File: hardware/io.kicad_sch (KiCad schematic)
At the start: 0 parts

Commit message: Almost everything
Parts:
- added D1, D3: 1N4007, Diode_THT:D_DO-41_SOD81_P10.16mm_Horizontal, symbol Diode:1N4007
- added Q4, Q5: NPN, symbol Simulation_SPICE:NPN
- added R27, R29, R33, R34: 1k, symbol Device:R
- added R28, R30: 10k, symbol Device:R
- added R31, R32: 1.2k, symbol Device:R
- added RLY1, RLY2: G5NB-1A-E-DC12, EasyEDA:RELAY-TH_G5NB-1A-E-DCXX, symbol EasyEDA:G5NB-1A-E-DC12
- added U24, U25: Optocoupler, symbol Isolator:Optocoupler_DC_PhotoNPN_AKEC
- added U26, U27: KF301-5.0-2P, EasyEDA:CONN-TH_P5.00_KF301-5.0-2P, symbol EasyEDA:KF301-5.0-2P
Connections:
- new net: Q5.2 (B), R29.2, R30.2
- new net: R31.1, U24.1
- new net: R31.2, U26.2
- new net: D1.2 (A), Q4.1 (C), RLY1.1
- new net: U25.2, U27.1
- new net: R32.2, U27.2
- new net: U24.2, U26.1
- new net: Q4.2 (B), R27.2, R28.2
- new net: D3.2 (A), Q5.1 (C), RLY2.1
- new net: R32.1, U25.1
- new net +12V: D1.1 (K), D3.1 (K), RLY1.4, RLY2.4
- new net +24V: RLY1.3, RLY2.3
- new net +3.3V: U24.3, U25.3
- new net DIN_2: R33.2, R34.2, U24.4, U25.4
- new net DOOUT_2: R29.1
- new net DOUT_1: R27.1
- new net GND: Q4.3 (E), Q5.3 (E), R28.1, R30.1, R33.1, R34.1, RLY1.2, RLY2.2
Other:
- note added: "24V INPUT"

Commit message: Board complete
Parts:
- removed D1, D3: 1N4007, Diode_THT:D_DO-41_SOD81_P10.16mm_Horizontal, symbol Diode:1N4007
- removed Q4, Q5: NPN, symbol Simulation_SPICE:NPN
- removed R31, R32: 1.2k, symbol Device:R
- removed U24, U25: Optocoupler, symbol Isolator:Optocoupler_DC_PhotoNPN_AKEC
- removed U26, U27: KF301-5.0-2P, EasyEDA:CONN-TH_P5.00_KF301-5.0-2P, symbol EasyEDA:KF301-5.0-2P
- added D2, D3, D6: 1N4148W, Samacsys:SODFL3816X120N, symbol Samacsys:1N4148W
- added D4, D5, D7: 1N4007W-T, Samacsys:SODFL3818X130N, symbol Samacsys:1N4007W-T
- added J14, J7: TB006-508-03BE, Samacsys:TB00650803BE, symbol Samacsys:TB006-508-03BE
- added Q1, Q2, Q3: 2N7002, EasyEDA:SOT-23-3_L2.9-W1.3-P1.90-LS2.4-BR, symbol EasyEDA:2N7002
- added R13, R14, R19: 3.3k, Resistor_SMD:R_1206_3216Metric_Pad1.30x1.75mm_HandSolder, symbol Device:R
- added R15: 330, Resistor_SMD:R_1206_3216Metric_Pad1.30x1.75mm_HandSolder, symbol Device:R
- added R16, R17, R6, R7: 10k, Resistor_SMD:R_1206_3216Metric_Pad1.30x1.75mm_HandSolder, symbol Device:R
- added R18: 20k, Resistor_SMD:R_1206_3216Metric_Pad1.30x1.75mm_HandSolder, symbol Device:R
- added RLY3: G5NB-1A-E-DC12, EasyEDA:RELAY-TH_G5NB-1A-E-DCXX, symbol EasyEDA:G5NB-1A-E-DC12
- added U10, U12, U4, U5, U8, U9: FUSE_C, Samacsys:01110501Z, symbol Samacsys:01110501Z
- added U11, U6, U7: LTV-814S-TA1, EasyEDA:SMD-4_L4.6-W6.5-P2.54-LS10.2-BL, symbol EasyEDA:LTV-814S-TA1
- R10: renamed from R28; footprint (none) -> Resistor_SMD:R_1206_3216Metric_Pad1.30x1.75mm_HandSolder
- R11: renamed from R34; value 1k -> 20k; footprint (none) -> Resistor_SMD:R_1206_3216Metric_Pad1.30x1.75mm_HandSolder
- R12: renamed from R33; value 1k -> 20k; footprint (none) -> Resistor_SMD:R_1206_3216Metric_Pad1.30x1.75mm_HandSolder
- R5: renamed from R29; value 1k -> 330; footprint (none) -> Resistor_SMD:R_1206_3216Metric_Pad1.30x1.75mm_HandSolder
- R8: renamed from R27; value 1k -> 330; footprint (none) -> Resistor_SMD:R_1206_3216Metric_Pad1.30x1.75mm_HandSolder
- R9: renamed from R30; footprint (none) -> Resistor_SMD:R_1206_3216Metric_Pad1.30x1.75mm_HandSolder
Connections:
- net +12V: now also D2.1 (K), D3.1 (K), D6.1 (K), RLY3.4
- net +24V: now also D4.2 (A), D5.2 (A), D7.2 (A); no longer RLY1.3, RLY2.3
- net DIN_2: now also R17.2, R18.2; no longer R11.2, R12.2
- net DOUT_1: now also R15.1; no longer R8.1
- net GND: now also Q1.2 (S), Q2.2 (S), Q3.2 (S), R16.1, R18.1, U11.2, U6.2, U7.2; no longer RLY1.2, RLY2.2
- net at R5.2, R9.2: now also Q1.1 (G)
- net at RLY1.1: now also D3.2 (A), Q2.3 (D)
- net at R10.2, R8.2: now also Q2.1 (G)
- net at RLY2.1: now also D2.2 (A), Q1.3 (D)
- net DOOUT_2 renamed DOUT_2
- new net: D5.1 (K), U9.1, U9.2
- new net: RLY2.3, U5.1, U5.2
- new net: D7.1 (K), U12.1, U12.2
- new net: RLY1.3, U4.1, U4.2
- new net: R7.1, U7.3
- new net: R14.2, U7.1
- new net: Q3.1 (G), R15.2, R16.2
- new net: D6.2 (A), Q3.3 (D), RLY3.1
- new net: R17.1, U11.3
- new net: R19.2, U11.1
- new net: R6.1, U6.3
- new net: R13.2, U6.1
- new net: RLY3.3, U10.1, U10.2
- new net: D4.1 (K), U8.1, U8.2
- new net +5V: U11.4, U6.4, U7.4
- new net DIN_1: R12.2, R7.2
- new net DIN_3: R11.2, R6.2
- new net DI_1: J14.1, R13.1
- new net DI_2: J14.2, R19.1
- new net DI_3: J14.3, R14.1
- new net DOUT_3: R8.1
- new net DO_1: J7.1, RLY1.2
- new net DO_2: J7.2, RLY2.2
- new net DO_3: J7.3, RLY3.2
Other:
- moved on the sheet: R10, R11, R12, R5, R8, R9, RLY1, RLY2

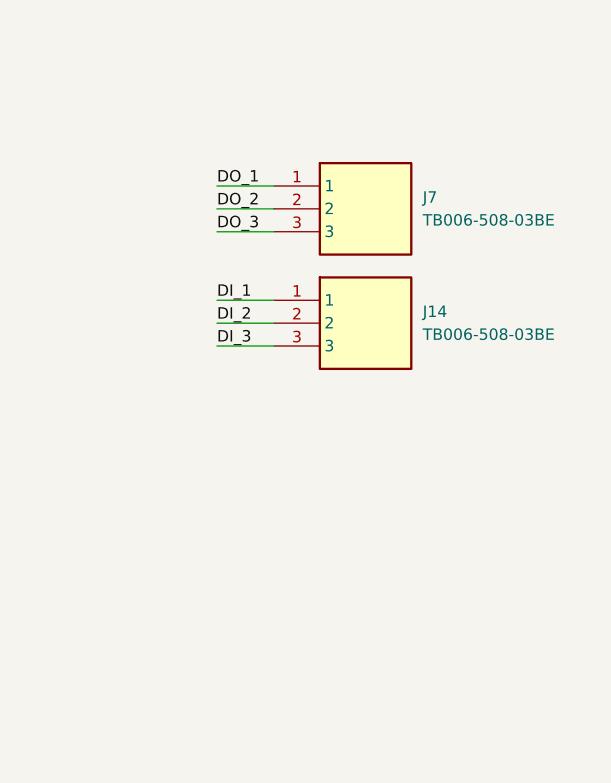
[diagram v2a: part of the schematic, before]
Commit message: Modbus, small schematic changes
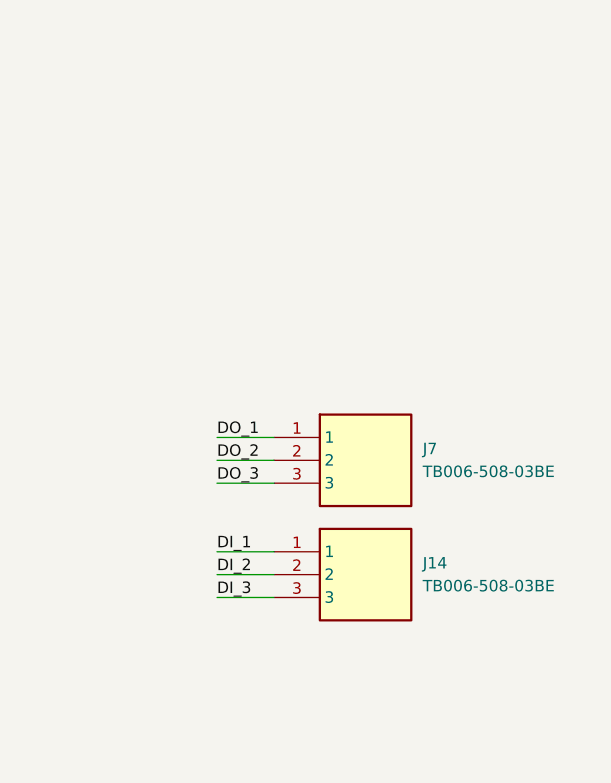
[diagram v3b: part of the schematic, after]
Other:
- moved on the sheet: J14, J7
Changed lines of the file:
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@@
 	(wire
 		(pts
-			(xy 233.68 118.11) (xy 240.03 118.11)
+			(xy 233.68 146.05) (xy 240.03 146.05)
 		)
 		(stroke
@@
 	(wire
 		(pts
-			(xy 233.68 125.73) (xy 240.03 125.73)
+			(xy 233.68 153.67) (xy 240.03 153.67)
 		)
 		(stroke
@@
 	(wire
 		(pts
-			(xy 233.68 130.81) (xy 240.03 130.81)
+			(xy 233.68 158.75) (xy 240.03 158.75)
 		)
 		(stroke
@@
 	(wire
 		(pts
-			(xy 233.68 128.27) (xy 240.03 128.27)
+			(xy 233.68 156.21) (xy 240.03 156.21)
 		)
 		(stroke
@@
 	(wire
 		(pts
-			(xy 233.68 115.57) (xy 240.03 115.57)
+			(xy 233.68 143.51) (xy 240.03 143.51)
 		)
 		(stroke
@@
 	(wire
 		(pts
-			(xy 233.68 113.03) (xy 240.03 113.03)
+			(xy 233.68 140.97) (xy 240.03 140.97)
 		)
 		(stroke
@@
 	)
 	(label "DO_2"
-		(at 233.68 115.57 0)
+		(at 233.68 143.51 0)
 		(effects
 			(font
@@
 	)
 	(label "DI_2"
-		(at 233.68 128.27 0)
+		(at 233.68 156.21 0)
 		(effects
 			(font
@@
 	)
 	(label "DI_1"
-		(at 233.68 125.73 0)
+		(at 233.68 153.67 0)
 		(effects
 			(font
@@
 	)
 	(label "DI_3"
-		(at 233.68 130.81 0)
+		(at 233.68 158.75 0)
 		(effects
 			(font
@@
 	)
 	(label "DO_3"
-		(at 233.68 118.11 0)
+		(at 233.68 146.05 0)
 		(effects
 			(font
@@
 	)
 	(label "DO_1"
-		(at 233.68 113.03 0)
+		(at 233.68 140.97 0)
 		(effects
 			(font
@@
 	(symbol
 		(lib_id "Samacsys:TB006-508-03BE")
-		(at 240.03 125.73 0)
+		(at 240.03 153.67 0)
 		(unit 1)
 		(exclude_from_sim no)
@@
 		(fields_autoplaced yes)
 		(property "Reference" "J14"
-			(at 256.54 126.9999 0)
+			(at 256.54 154.9399 0)
 			(effects
 				(font
@@
 		)
 		(property "Value" "TB006-508-03BE"
-			(at 256.54 129.5399 0)
+			(at 256.54 157.4799 0)
 			(effects
 				(font
@@
 		)
 		(property "Footprint" "Samacsys:TB00650803BE"
-			(at 256.54 220.65 0)
+			(at 256.54 248.59 0)
 			(effects
 				(font
@@
 		)
 		(property "Datasheet" "https://www.sameskydevices.com/product/resource/supplyframepdf/tb006-508.pdf"
-			(at 256.54 320.65 0)
+			(at 256.54 348.59 0)
 			(effects
 				(font
@@
 		)
 		(property "Description" "2~24 Poles, Screw Type, Horizontal, 5.08 Pitch, 26~14 (AWG), Terminal Block Connector"
-			(at 240.03 125.73 0)
+			(at 240.03 153.67 0)
 			(effects
 				(font
@@
 		)
 		(property "Height" "10.4"
-			(at 256.54 520.65 0)
+			(at 256.54 548.59 0)
 			(effects
 				(font
@@
 		)
 		(property "Mouser Part Number" "490-TB006-508-03BE"
-			(at 256.54 620.65 0)
+			(at 256.54 648.59 0)
 			(effects
 				(font
@@
 		)
 		(property "Mouser Price/Stock" "https://www.mouser.co.uk/ProductDetail/Same-Sky/TB006-508-03BE?qs=vLWxofP3U2zmvvLYJBQLMA%3D%3D"
-			(at 256.54 720.65 0)
+			(at 256.54 748.59 0)
 			(effects
 				(font
@@
 		)
 		(property "Manufacturer_Name" "Same Sky"
-			(at 256.54 820.65 0)
+			(at 256.54 848.59 0)
 			(effects
 				(font
@@
 		)
 		(property "Manufacturer_Part_Number" "TB006-508-03BE"
-			(at 256.54 920.65 0)
+			(at 256.54 948.59 0)
 			(effects
 				(font
@@
 	(symbol
 		(lib_id "Samacsys:TB006-508-03BE")
-		(at 240.03 113.03 0)
+		(at 240.03 140.97 0)
 		(unit 1)
 		(exclude_from_sim no)
@@
 		(fields_autoplaced yes)
 		(property "Reference" "J7"
-			(at 256.54 114.2999 0)
+			(at 256.54 142.2399 0)
 			(effects
 				(font
@@
 		)
 		(property "Value" "TB006-508-03BE"
-			(at 256.54 116.8399 0)
+			(at 256.54 144.7799 0)
 			(effects
 				(font
@@
 		)
 		(property "Footprint" "Samacsys:TB00650803BE"
-			(at 256.54 207.95 0)
+			(at 256.54 235.89 0)
 			(effects
 				(font
@@
 		)
 		(property "Datasheet" "https://www.sameskydevices.com/product/resource/supplyframepdf/tb006-508.pdf"
-			(at 256.54 307.95 0)
+			(at 256.54 335.89 0)
 			(effects
 				(font
@@
 		)
 		(property "Description" "2~24 Poles, Screw Type, Horizontal, 5.08 Pitch, 26~14 (AWG), Terminal Block Connector"
-			(at 240.03 113.03 0)
+			(at 240.03 140.97 0)
 			(effects
 				(font
@@
 		)
 		(property "Height" "10.4"
-			(at 256.54 507.95 0)
+			(at 256.54 535.89 0)
 			(effects
 				(font
@@
 		)
 		(property "Mouser Part Number" "490-TB006-508-03BE"
-			(at 256.54 607.95 0)
+			(at 256.54 635.89 0)
 			(effects
 				(font
@@
 		)
 		(property "Mouser Price/Stock" "https://www.mouser.co.uk/ProductDetail/Same-Sky/TB006-508-03BE?qs=vLWxofP3U2zmvvLYJBQLMA%3D%3D"
-			(at 256.54 707.95 0)
+			(at 256.54 735.89 0)
 			(effects
 				(font
@@
 		)
 		(property "Manufacturer_Name" "Same Sky"
-			(at 256.54 807.95 0)
+			(at 256.54 835.89 0)
 			(effects
 				(font
@@
 		)
 		(property "Manufacturer_Part_Number" "TB006-508-03BE"
-			(at 256.54 907.95 0)
+			(at 256.54 935.89 0)
 			(effects
 				(font

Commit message: UART parity and better timing handling
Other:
- title: (none) -> Digital IO
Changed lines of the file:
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@@
 	(generator_version "9.0")
 	(paper "A4")
+	(title_block
+		(title "Digital IO")
+	)
 	(text "24V INPUT"
 		(exclude_from_sim no)
